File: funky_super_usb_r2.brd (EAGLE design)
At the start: 21.8 x 22.6 mm, 28 parts, among them IC1 TINY24/44/84-SSU, IC2 LTC3525, IC3 MCP1703CB, X1 USB-MICROB

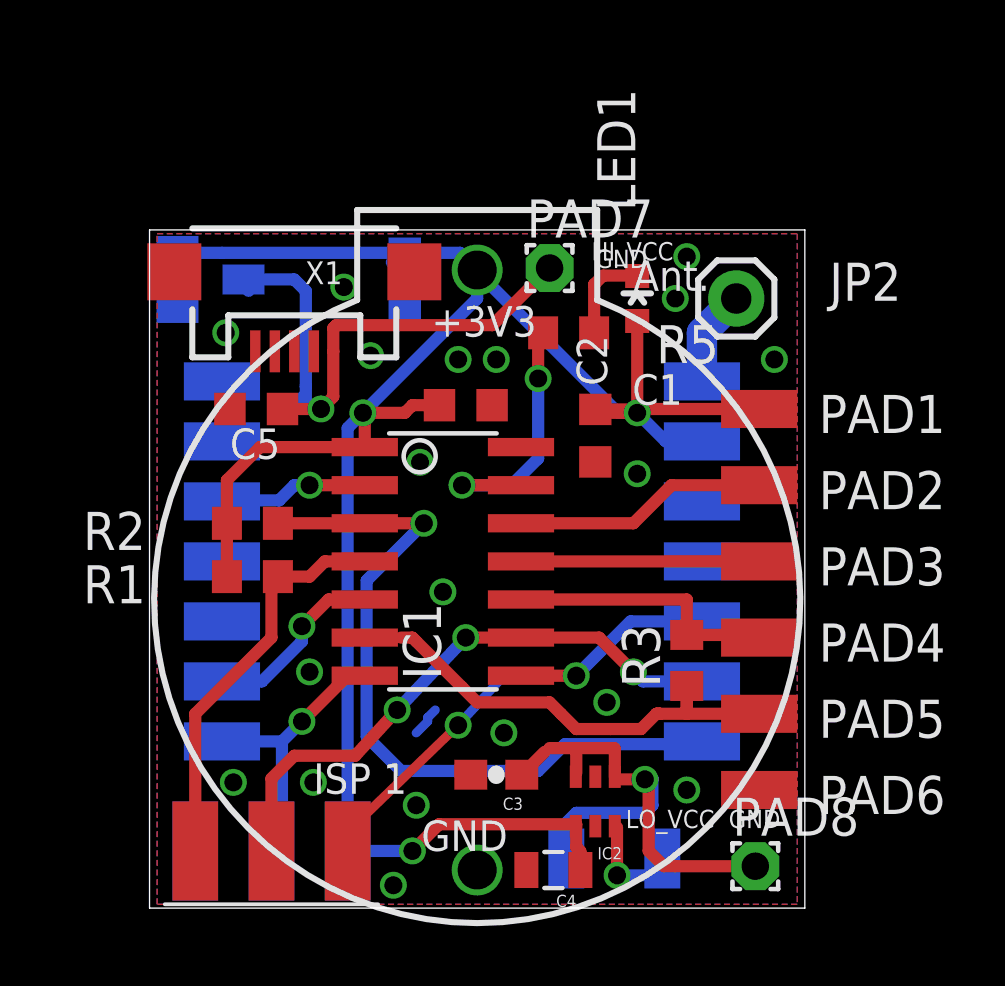
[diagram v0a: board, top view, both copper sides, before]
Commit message: edited silk and reduced vias
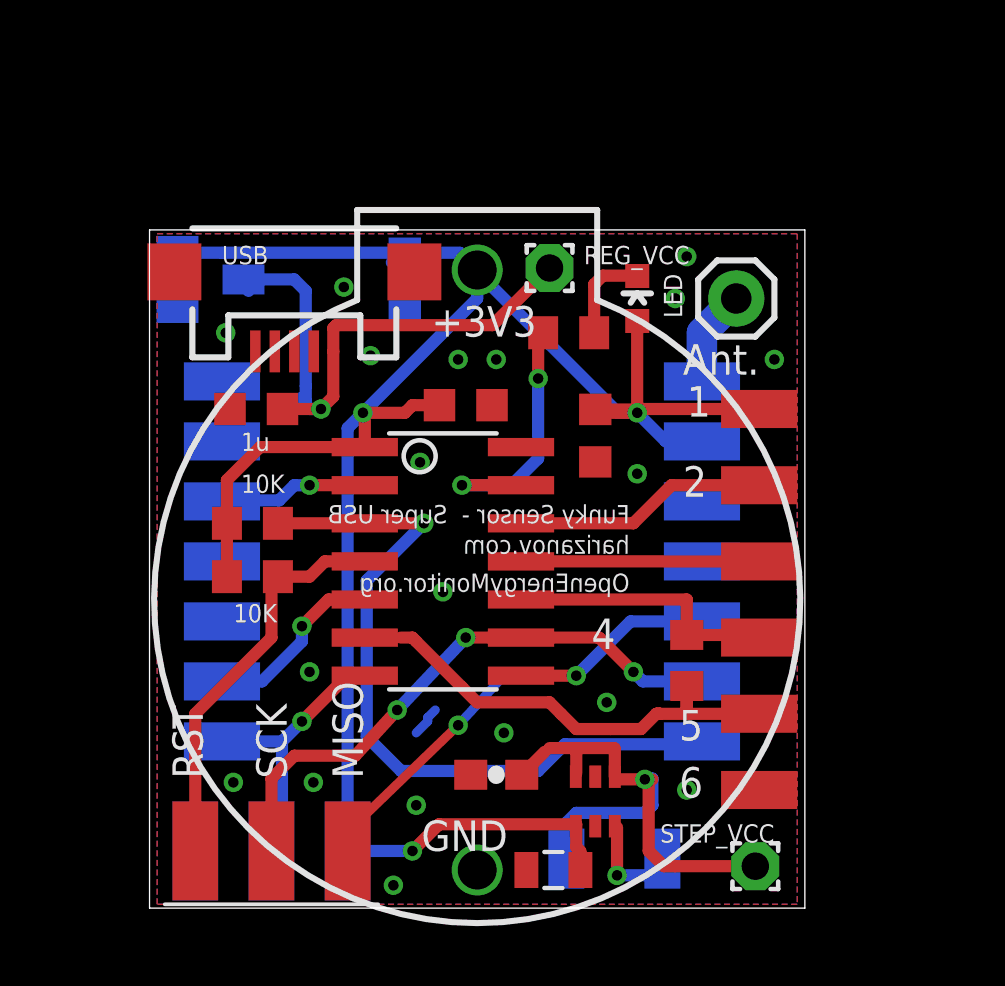
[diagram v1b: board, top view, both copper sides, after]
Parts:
- IC1: value TINY24/44/84-SSU -> Attiny84
- renumbered LED1 to LED, U$1 to RFM12B
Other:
- board text added: "1"
- board text added: "10K"
- board text added: "1u"
- board text added: "2"
- board text added: "4"
- board text added: "5"
- board text added: "6"
- board text added: "Funky Sensor - Super USB"
- board text added: "MISO"
- board text added: "OpenEnergyMonitor.org"
- board text added: "REG_VCC"
- board text added: "RST"
- board text added: "SCK"
- board text added: "STEP_VCC"
- board text added: "USB"
- board text added: "harizanov.com"
- board text removed: "HI_VCC"
- board text removed: "ISP 1"
- board text removed: "LO_VCC"
